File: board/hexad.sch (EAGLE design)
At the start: 89 parts, among them Q1 40V, U2 RADIO-ESP32_DEVKIT, U3 R-78E5.0-1.0

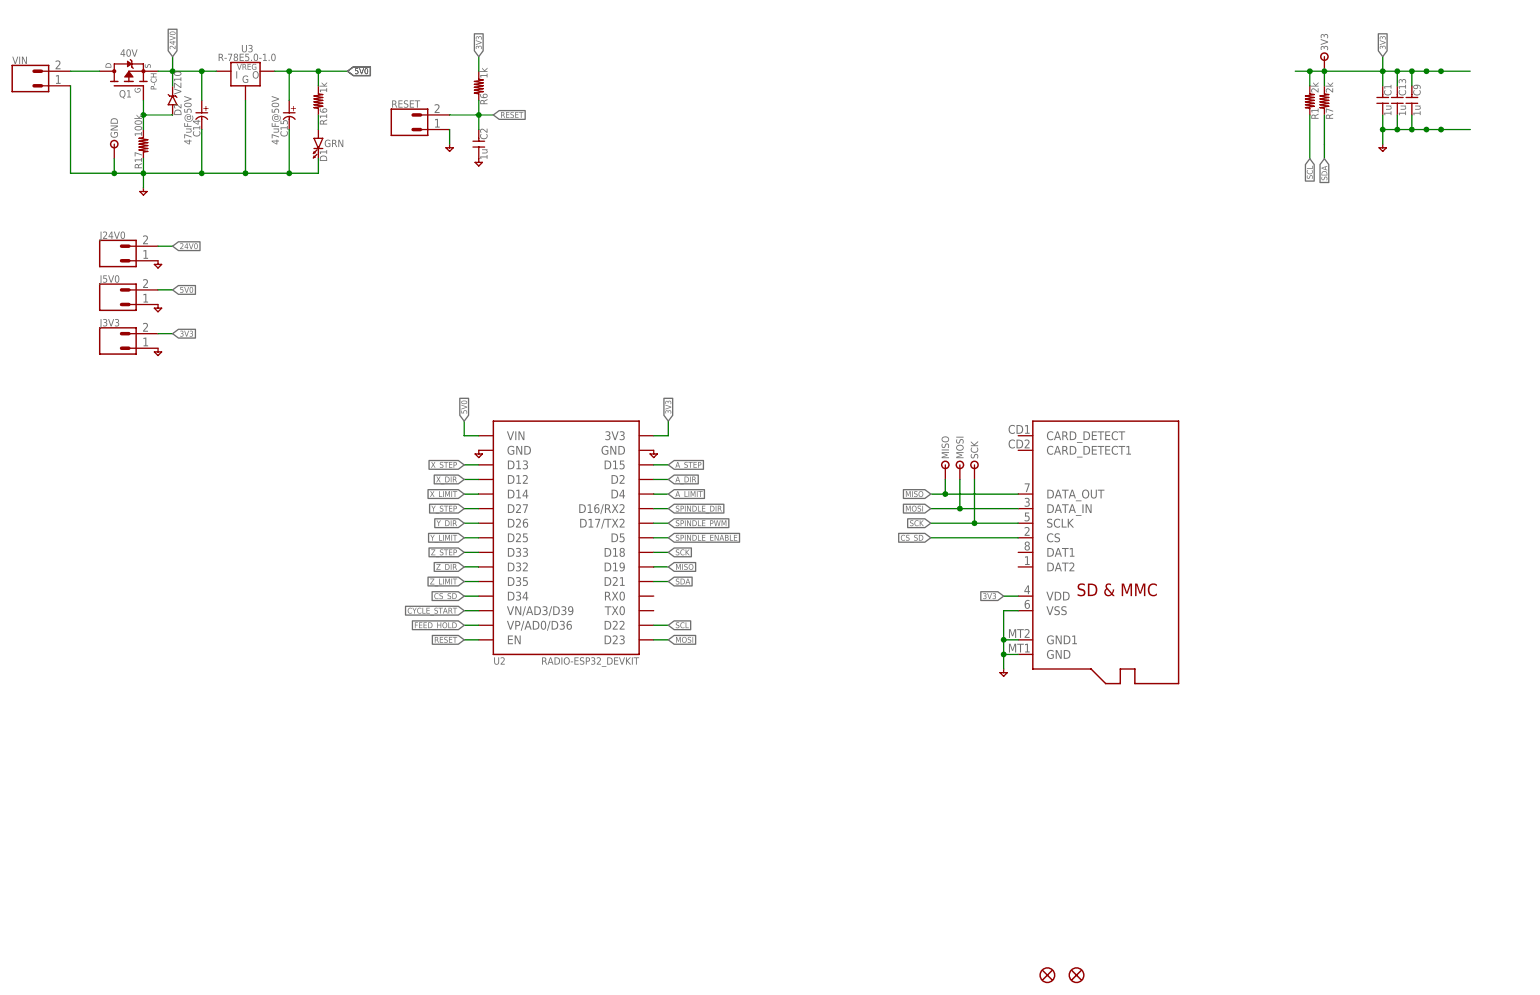
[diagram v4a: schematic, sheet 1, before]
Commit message: added todo to schematic
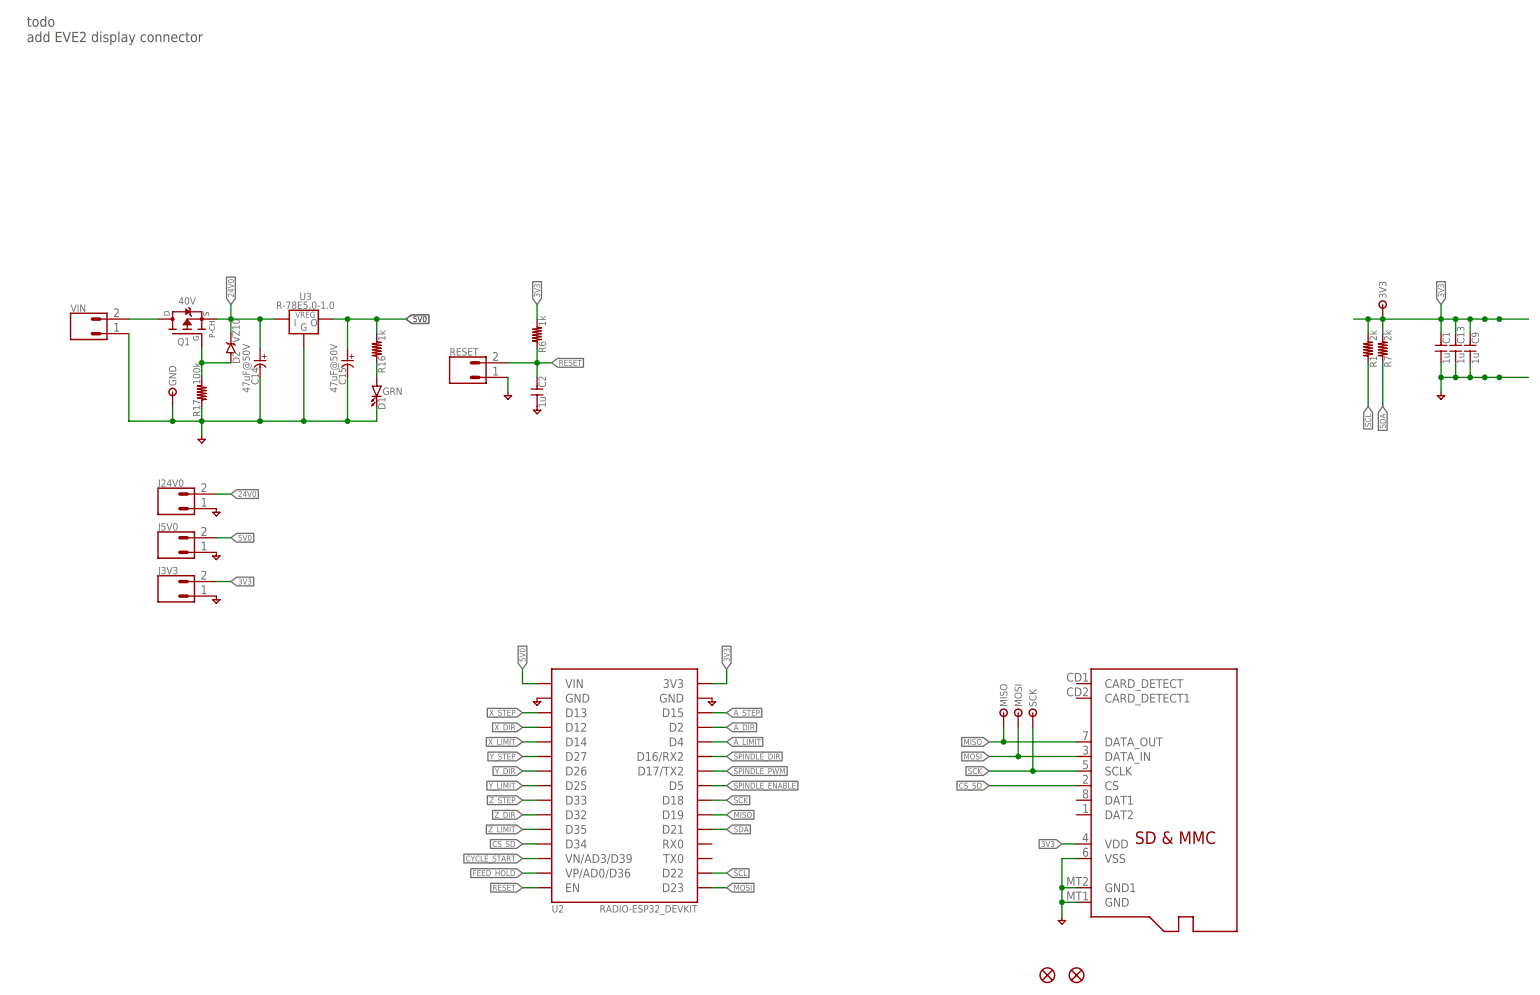
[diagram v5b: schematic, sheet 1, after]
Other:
- note added: "todo add EVE2 display connector"
- moved on the sheet: 3V3, C1, C13, C14, C15, C2, C9, D1, D2, GND, J24V0, J3V3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
